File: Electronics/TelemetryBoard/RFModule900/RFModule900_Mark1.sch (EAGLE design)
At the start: 166 parts, among them T1 DC08-73, T2 DC08-73, U1 TPS2561, U2 TPS2561, U3 LM75B, U4 LTC5505, U5 LTC5505, U6 MCP4728, U7 ADC128D818, U8 MIC5504-3.3YM5, U9 TCA9535, Y1 30 Mhz

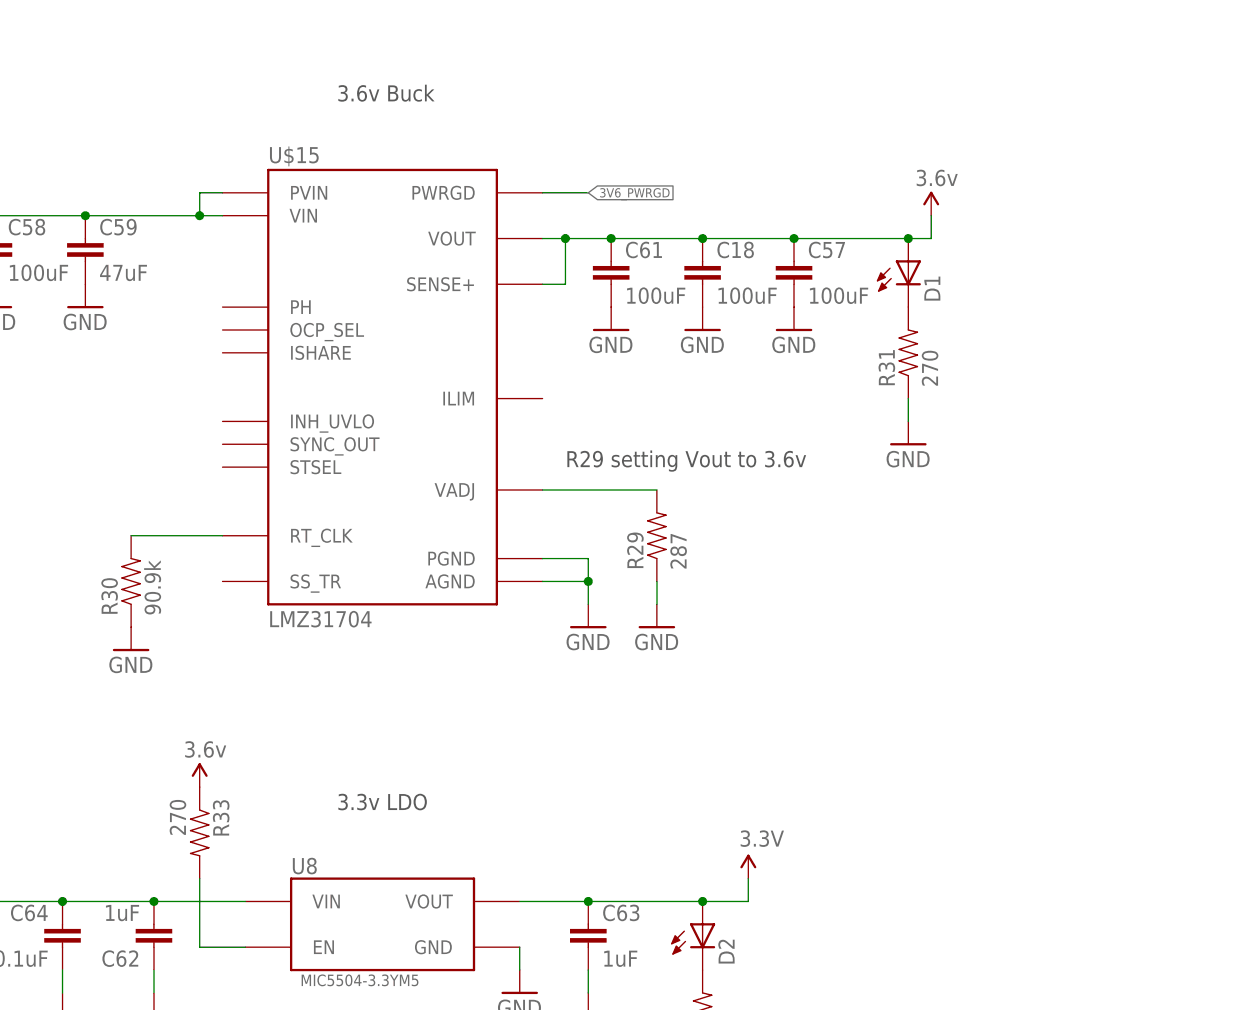
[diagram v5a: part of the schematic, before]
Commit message: adding backround info about modules
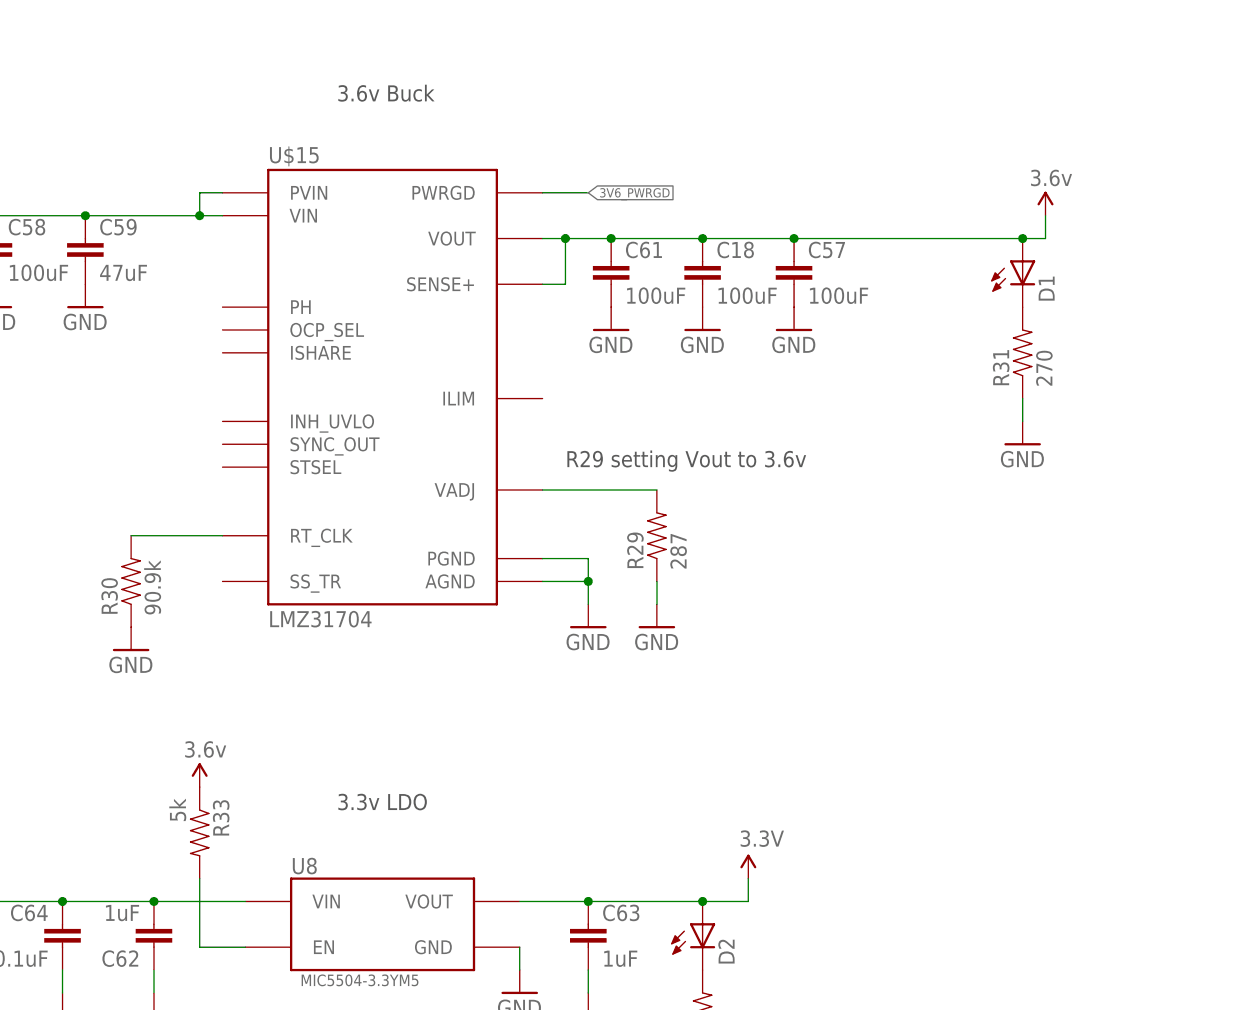
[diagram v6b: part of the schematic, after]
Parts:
- R33: value 270 -> 5k
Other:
- moved on the sheet: D1, R31
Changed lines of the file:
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@@
 <part name="GND92" library="SparkFun-Aesthetics" deviceset="GND" device=""/>
 <part name="GND93" library="SparkFun-Aesthetics" deviceset="GND" device=""/>
-<part name="R33" library="SparkFun-Resistors" deviceset="RESISTOR" device="0402-RES" value="270"/>
+<part name="R33" library="SparkFun-Resistors" deviceset="RESISTOR" device="0402-RES" value="5k"/>
 <part name="U$19" library="RitLaunchInitiative" deviceset="3.6V" device=""/>
 <part name="C64" library="SparkFun-Capacitors" deviceset="CAP" device="0402-CAP" value="0.1uF">
@@
 <instance part="GND89" gate="1" x="-203.2" y="317.5"/>
 <instance part="GND90" gate="1" x="-193.04" y="317.5"/>
-<instance part="U$17" gate="G$1" x="-177.8" y="330.2"/>
+<instance part="U$17" gate="G$1" x="-165.1" y="330.2"/>
 <instance part="U$18" gate="G$1" x="-287.02" y="256.54"/>
 <instance part="C62" gate="G$1" x="-264.16" y="251.46" rot="R180">
@@
 <attribute name="MPN" x="-215.9" y="248.92" size="1.778" layer="96" display="off"/>
 </instance>
-<instance part="D1" gate="G$1" x="-180.34" y="325.12">
-<attribute name="DIGI" x="-180.34" y="325.12" size="1.778" layer="96" display="off"/>
-<attribute name="COLOR" x="-180.34" y="325.12" size="1.778" layer="96" display="off"/>
-</instance>
-<instance part="R31" gate="G$1" x="-180.34" y="314.96" rot="R90"/>
-<instance part="GND91" gate="1" x="-180.34" y="304.8"/>
+<instance part="D1" gate="G$1" x="-167.64" y="325.12">
+<attribute name="DIGI" x="-167.64" y="325.12" size="1.778" layer="96" display="off"/>
+<attribute name="COLOR" x="-167.64" y="325.12" size="1.778" layer="96" display="off"/>
+</instance>
+<instance part="R31" gate="G$1" x="-167.64" y="314.96" rot="R90"/>
+<instance part="GND91" gate="1" x="-167.64" y="304.8"/>
 <instance part="SUPPLY32" gate="G$1" x="-198.12" y="256.54"/>
 <instance part="D2" gate="G$1" x="-203.2" y="251.46">
@@
 <pinref part="GND91" gate="1" pin="GND"/>
 <pinref part="R31" gate="G$1" pin="1"/>
-<wire x1="-180.34" y1="309.88" x2="-180.34" y2="307.34" width="0.1524" layer="91"/>
+<wire x1="-167.64" y1="309.88" x2="-167.64" y2="307.34" width="0.1524" layer="91"/>
 </segment>
 <segment>
@@
 <wire x1="-213.36" y1="327.66" x2="-203.2" y2="327.66" width="0.1524" layer="91"/>
 <wire x1="-203.2" y1="327.66" x2="-193.04" y2="327.66" width="0.1524" layer="91"/>
-<wire x1="-193.04" y1="327.66" x2="-180.34" y2="327.66" width="0.1524" layer="91"/>
-<wire x1="-180.34" y1="327.66" x2="-177.8" y2="327.66" width="0.1524" layer="91"/>
+<wire x1="-193.04" y1="327.66" x2="-167.64" y2="327.66" width="0.1524" layer="91"/>
+<wire x1="-167.64" y1="327.66" x2="-165.1" y2="327.66" width="0.1524" layer="91"/>
 <wire x1="-220.98" y1="322.58" x2="-218.44" y2="322.58" width="0.1524" layer="91"/>
 <wire x1="-218.44" y1="322.58" x2="-218.44" y2="327.66" width="0.1524" layer="91"/>
@@
 <junction x="-193.04" y="327.66"/>
 <pinref part="U$17" gate="G$1" pin="3.6V"/>
-<wire x1="-177.8" y1="327.66" x2="-177.8" y2="330.2" width="0.1524" layer="91"/>
+<wire x1="-165.1" y1="327.66" x2="-165.1" y2="330.2" width="0.1524" layer="91"/>
 <pinref part="D1" gate="G$1" pin="A"/>
-<junction x="-180.34" y="327.66"/>
-</segment>
-<segment>
+<junction x="-167.64" y="327.66"/>
+</segment>
+<segment>
